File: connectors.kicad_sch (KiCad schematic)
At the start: 2 parts, among them J1 0436500200, J2 0430450200

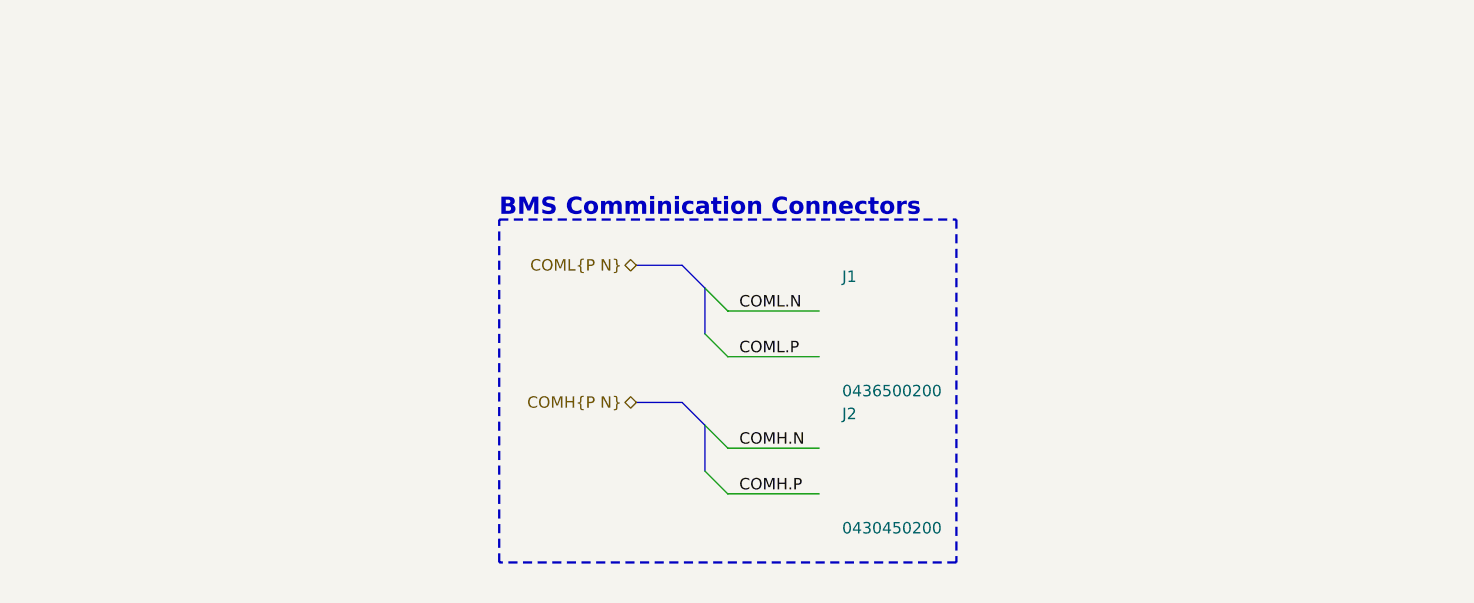
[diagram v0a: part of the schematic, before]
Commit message: SCH[Connector]: Added tim board to board connector.
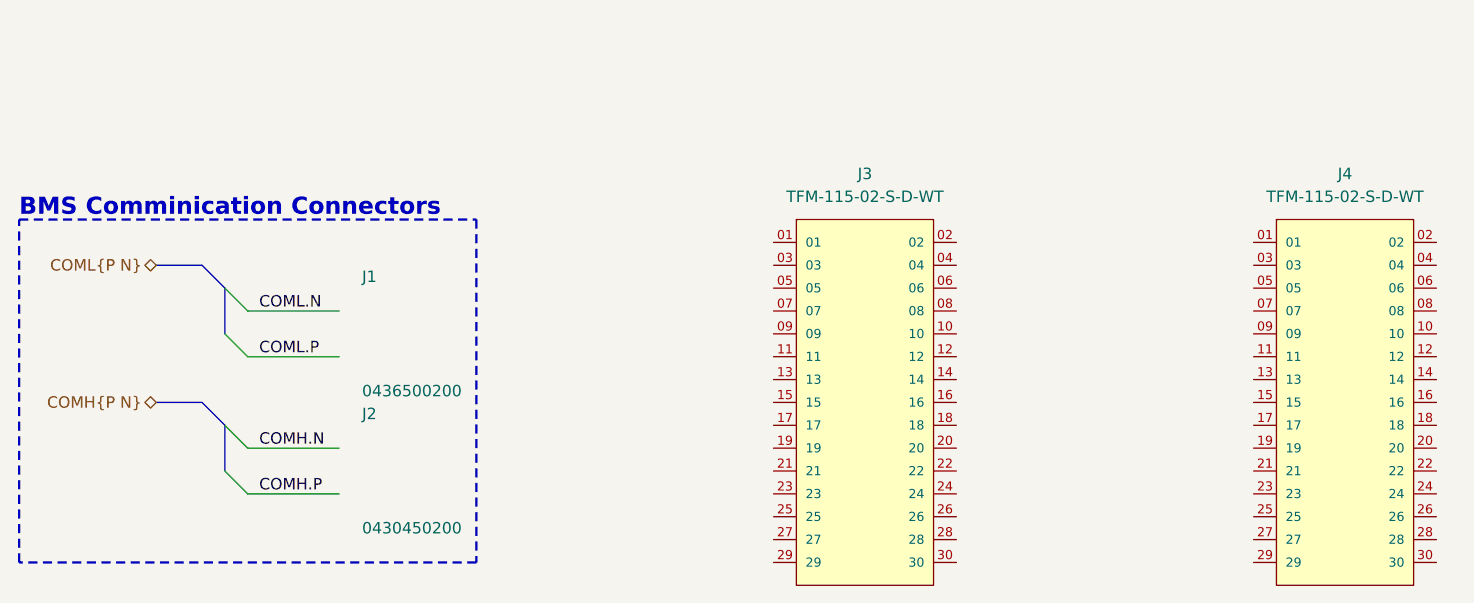
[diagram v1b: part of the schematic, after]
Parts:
- added J3, J4: TFM-115-02-S-D-WT, remote_tfm-115-02-s-d-wt:SAMTEC_TFM-115-02-S-D-WT, symbol remote_tfm-115-02-s-d-wt:TFM-115-02-S-D-WT

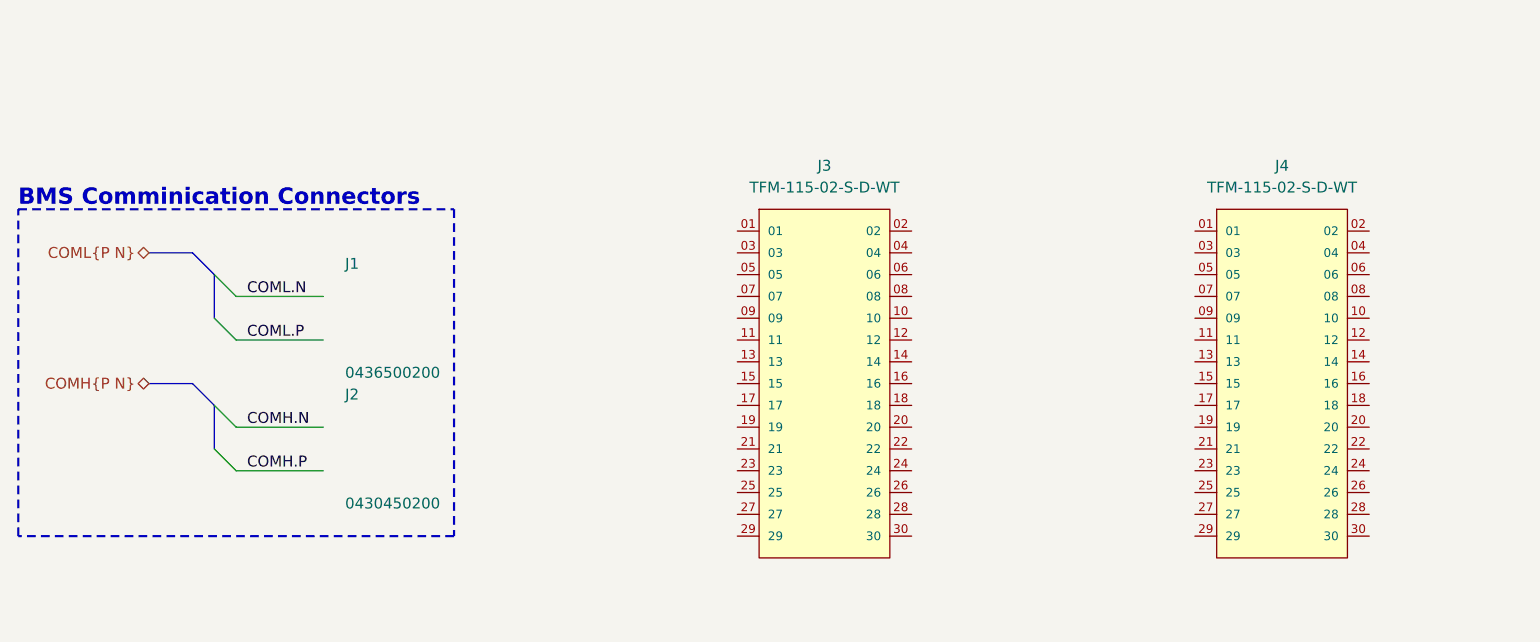
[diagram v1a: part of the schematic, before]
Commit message: SCH[Connecotr]: Added tim pinout.
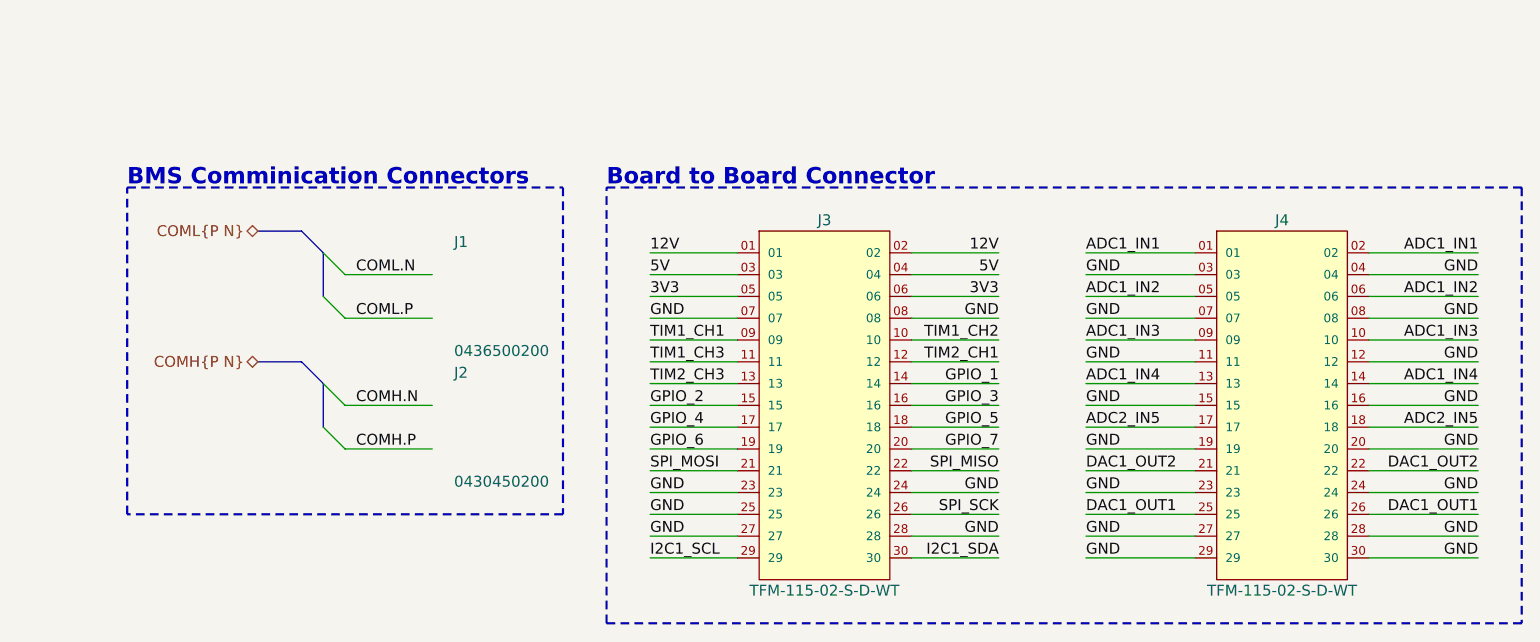
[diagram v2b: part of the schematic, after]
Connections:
- net ADC1_IN1: now reaches J4.01
- net ADC1_IN1: now also J4.02
- net GND: now reaches J4.03
- net GND: now also J3.07, J3.08, J3.23, J3.24, J3.25, J3.27, J3.28, J4.04, J4.07, J4.08, J4.11, J4.12, J4.15, J4.16, J4.19, J4.20, J4.23, J4.24, J4.27, J4.28, J4.29, J4.30
- net ADC1_IN2: now reaches J4.05
- net ADC1_IN2: now also J4.06
- net ADC1_IN3: now reaches J4.09
- net ADC1_IN3: now also J4.10
- net ADC1_IN4: now reaches J4.13
- net ADC1_IN4: now also J4.14
- net ADC2_IN5: now reaches J4.17
- net ADC2_IN5: now also J4.18
- net DAC1_OUT2: now reaches J4.21
- net DAC1_OUT2: now also J4.22
- net DAC1_OUT1: now reaches J4.25
- net DAC1_OUT1: now also J4.26
- net 12V: now reaches J3.01
- net 12V: now also J3.02
- net 5V: now reaches J3.03
- net 5V: now also J3.04
- net 3V3: now reaches J3.05
- net 3V3: now also J3.06
- net TIM1_CH1: now reaches J3.09
- net TIM1_CH2: now reaches J3.10
- net TIM1_CH3: now reaches J3.11
- net TIM2_CH1: now reaches J3.12
- net TIM2_CH3: now reaches J3.13
- net GPIO_1: now reaches J3.14
- net GPIO_2: now reaches J3.15
- net GPIO_3: now reaches J3.16
- net GPIO_4: now reaches J3.17
- net GPIO_5: now reaches J3.18
- net GPIO_6: now reaches J3.19
- net GPIO_7: now reaches J3.20
- net SPI_MOSI: now reaches J3.21
- net SPI_MISO: now reaches J3.22
- net SPI_SCK: now reaches J3.26
- net I2C1_SCL: now reaches J3.29
- net I2C1_SDA: now reaches J3.30
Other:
- note added: "Board to Board Connector"
- moved on the sheet: J3, J4

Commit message: SCH[Power]: Adding caps, resistors based off datasheet recs.
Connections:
- net 12V renamed +12V
- net 3V3 renamed +3V3
- net 5V renamed +5V
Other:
- note added: "Power"
- moved on the sheet: J3, J4

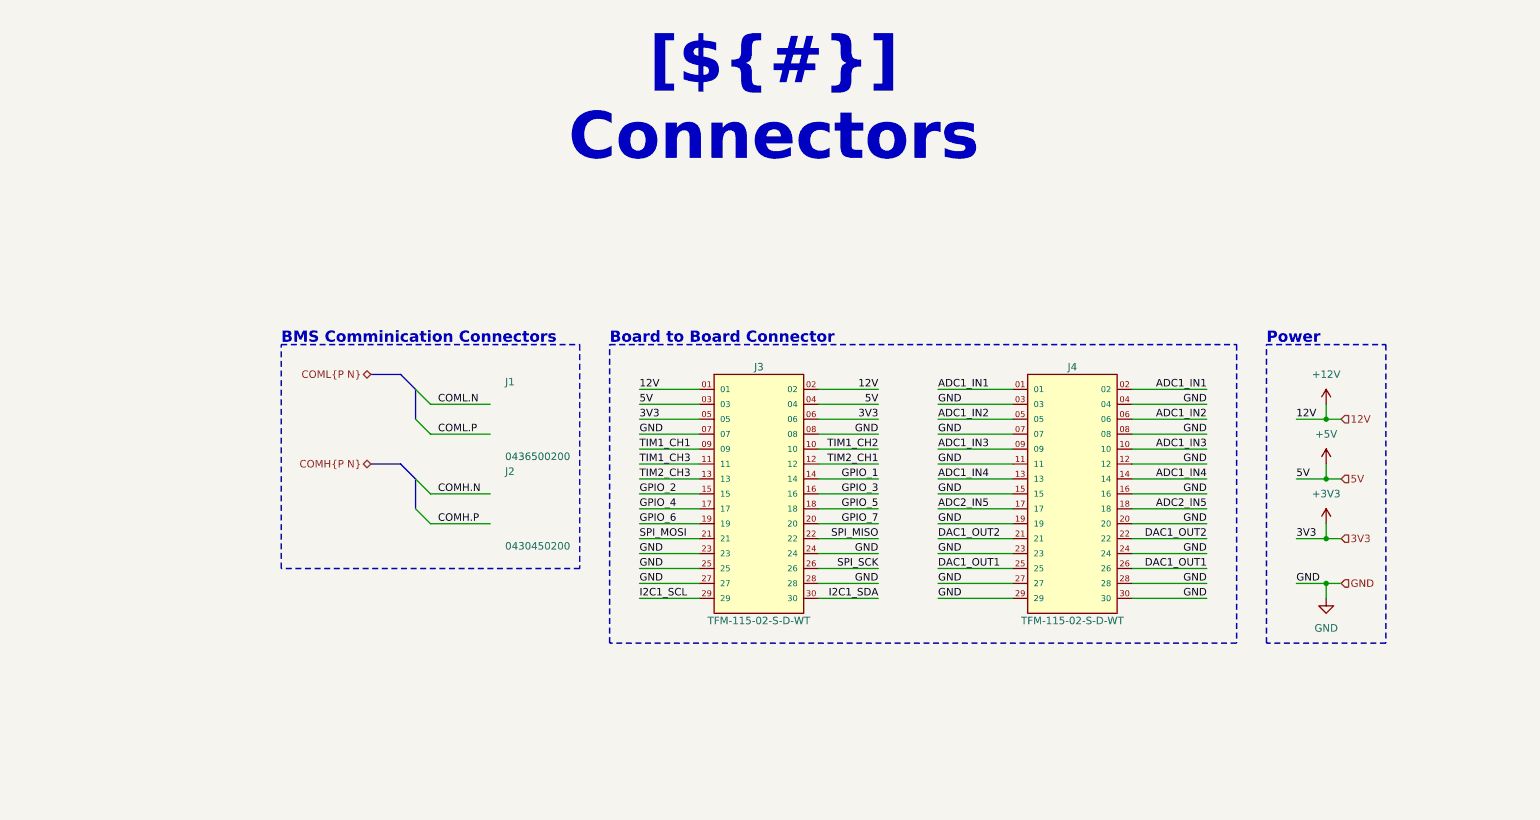
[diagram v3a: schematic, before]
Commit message: SCH[Pages, Chips]: Created page setup, and placed main IC's.
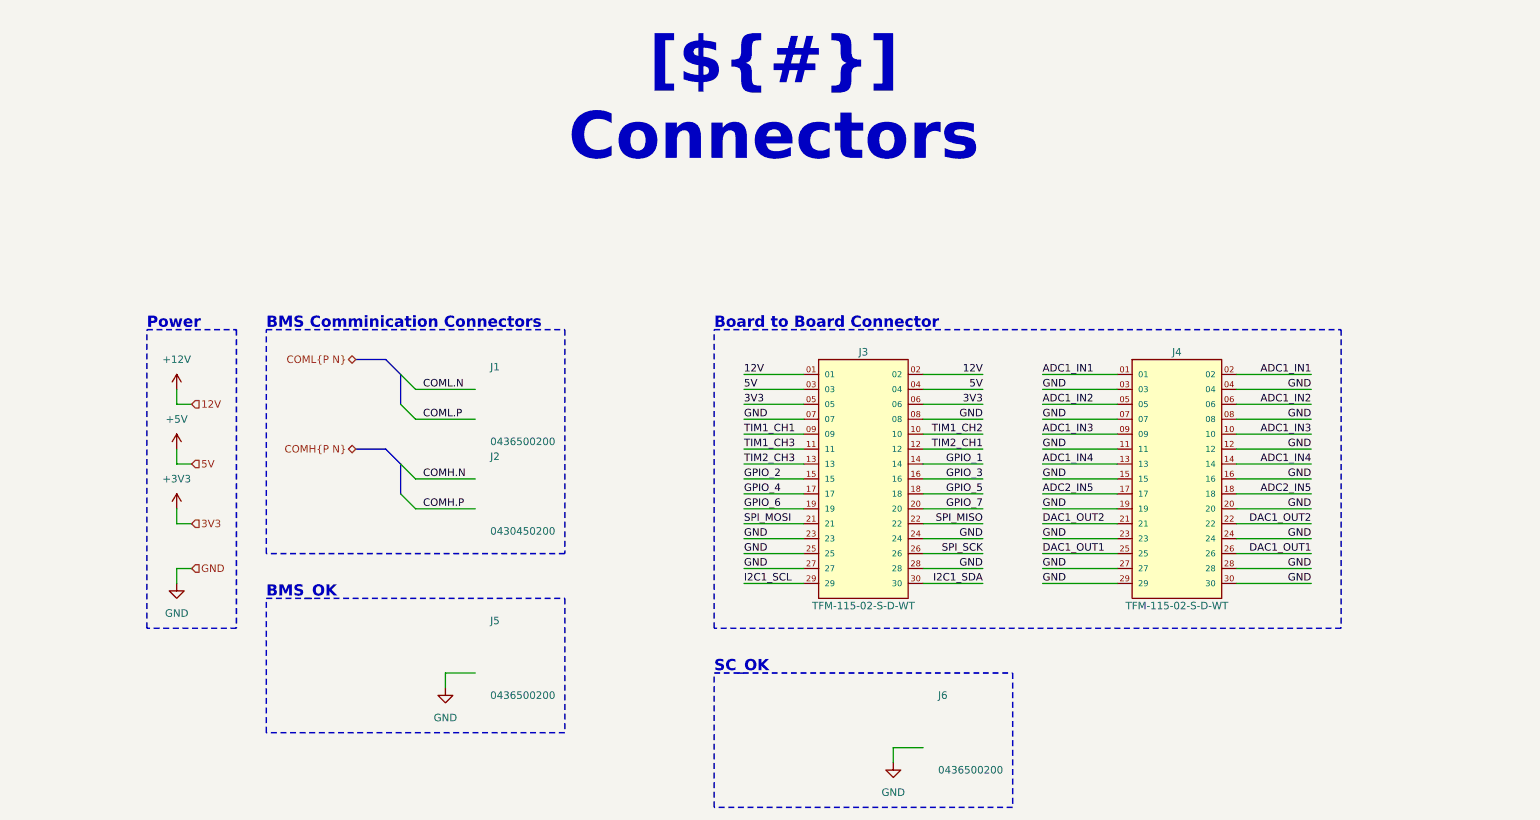
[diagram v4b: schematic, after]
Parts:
- added J5, J6: 0436500200, remote_0436500200:CONN_SD-43650-001_02_MOL, symbol remote_0436500200:0436500200
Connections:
- net GND: now also J5.2, J6.2
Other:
- note added: "BMS_OK"
- note added: "SC_OK"
- moved on the sheet: J3, J4

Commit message: SCH[Labels]: Working on pinout for tim.
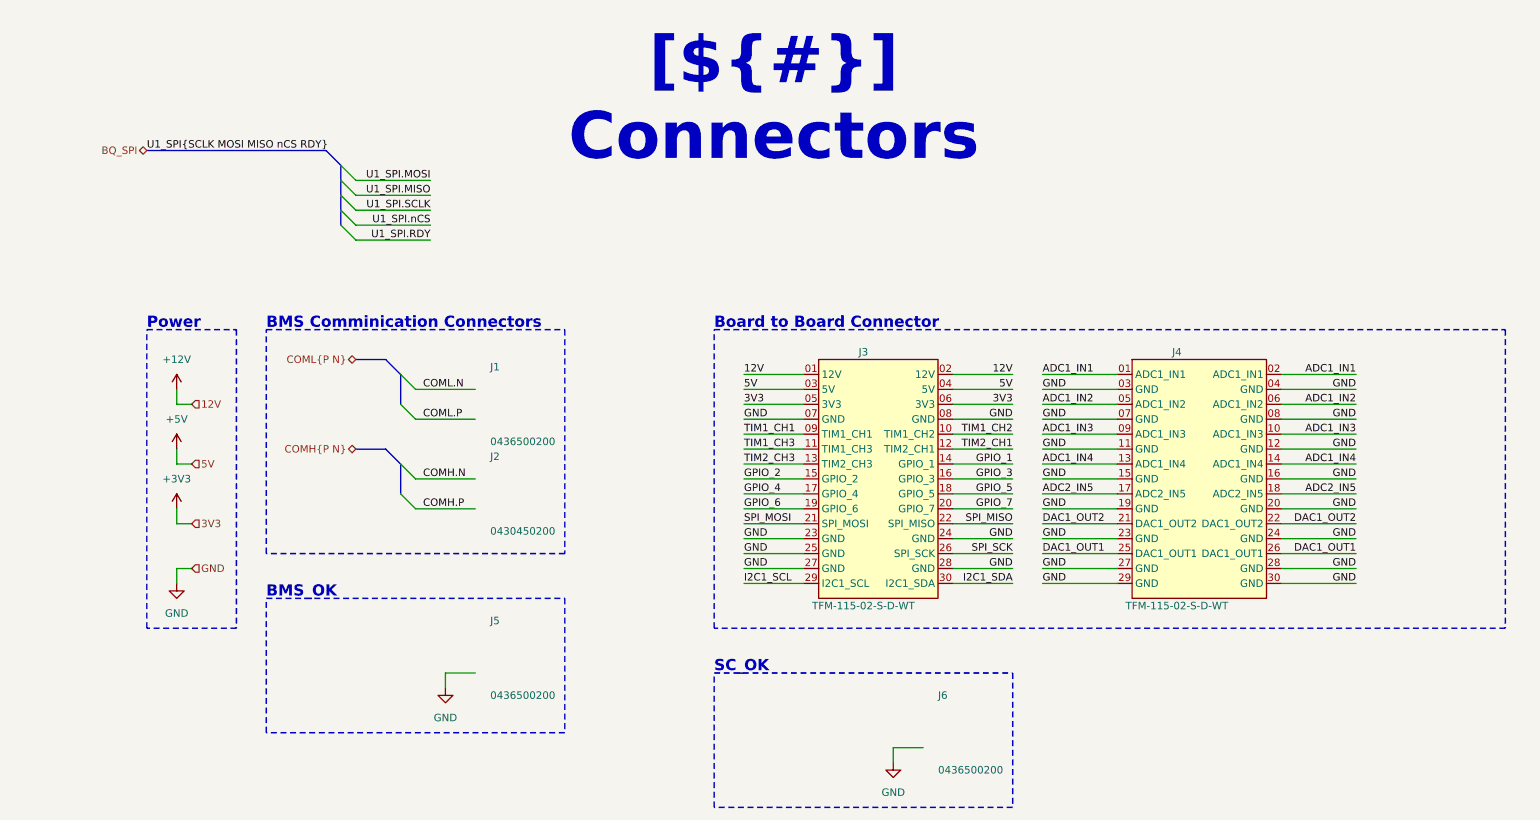
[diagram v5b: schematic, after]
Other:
- moved on the sheet: J3, J4

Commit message: SCH[Sens & Inputs, Logic]: Started on sens and inputs condtiong, Logic page drawn. Need to add notes still.
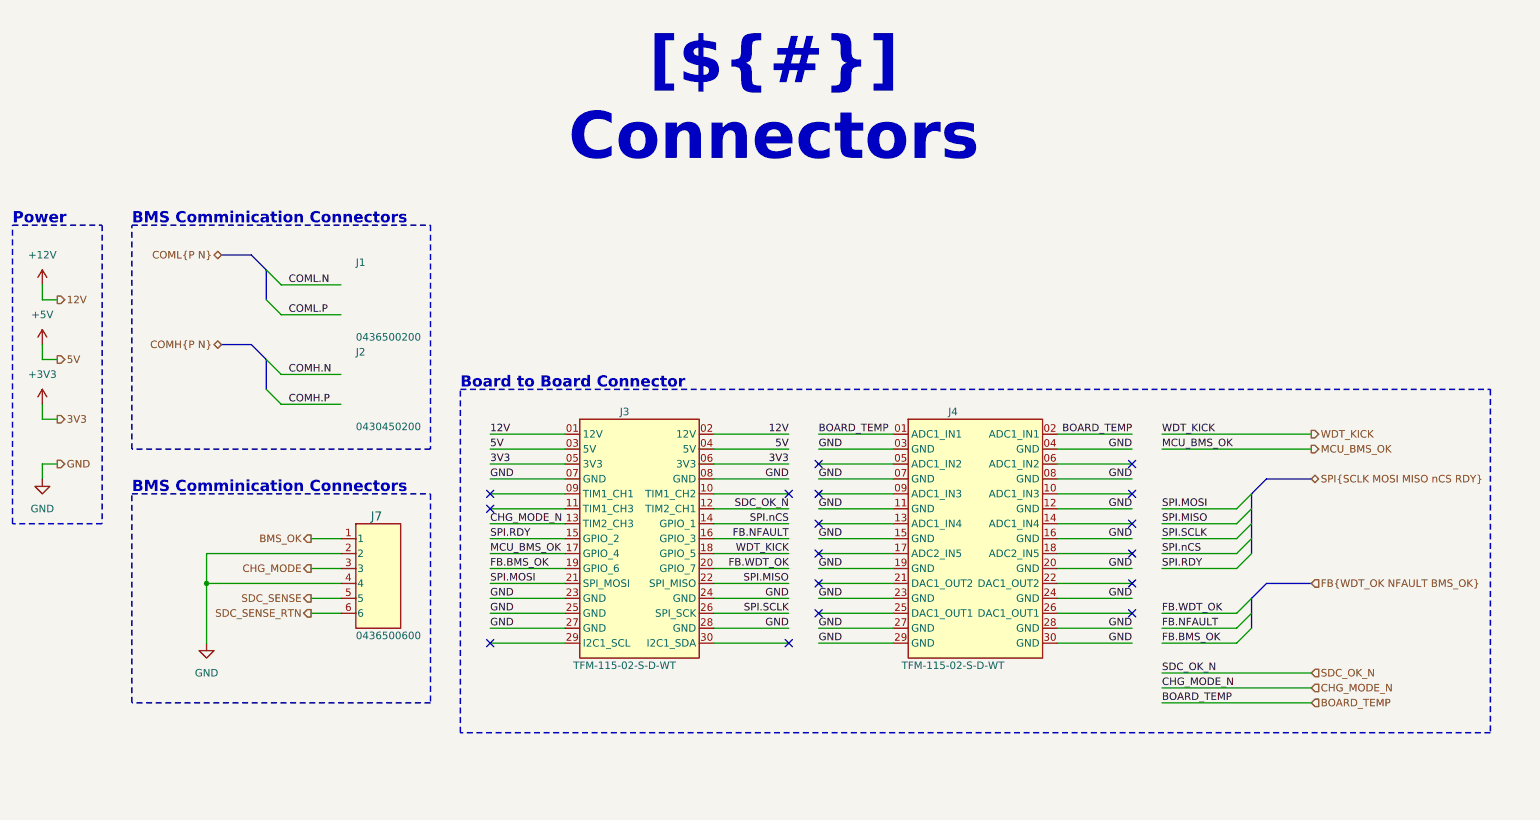
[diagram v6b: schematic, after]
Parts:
- removed J5, J6: 0436500200, remote_0436500200:CONN_SD-43650-001_02_MOL, symbol remote_0436500200:0436500200
- added J7: 0436500600, remote_0436500600:CONN_SD-43650-001_06_MOL, symbol remote_0436500600:0436500600
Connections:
- net GND: now also J7.2, J7.4
- net ADC1_IN1 renamed BOARD_TEMP
- net ADC1_IN2: no longer names the net of J4.05 (ADC1_IN2)
- net ADC1_IN2: no longer J4.06 (ADC1_IN2)
- net ADC1_IN3: no longer names the net of J4.09 (ADC1_IN3)
- net ADC1_IN3: no longer J4.10 (ADC1_IN3)
- net ADC1_IN4: no longer names the net of J4.13 (ADC1_IN4)
- net ADC1_IN4: no longer J4.14 (ADC1_IN4)
- net ADC2_IN5: no longer names the net of J4.17 (ADC2_IN5)
- net ADC2_IN5: no longer J4.18 (ADC2_IN5)
- net DAC1_OUT1: no longer names the net of J4.25 (DAC1_OUT1)
- net DAC1_OUT1: no longer J4.26 (DAC1_OUT1)
- net DAC1_OUT2: no longer names the net of J4.21 (DAC1_OUT2)
- net DAC1_OUT2: no longer J4.22 (DAC1_OUT2)
- net GPIO_1 renamed SPI.nCS
- net GPIO_2 renamed SPI.RDY
- net GPIO_3 renamed FB.NFAULT
- net GPIO_4 renamed MCU_BMS_OK
- net GPIO_5 renamed WDT_KICK
- net GPIO_6 renamed FB.BMS_OK
- net GPIO_7 renamed FB.WDT_OK
- net I2C1_SCL: no longer names the net of J3.29 (I2C1_SCL)
- net I2C1_SDA: no longer names the net of J3.30 (I2C1_SDA)
- net SPI_MISO renamed SPI.MISO
- net SPI_MOSI renamed SPI.MOSI
- net SPI_SCK renamed SPI.SCLK
- net TIM1_CH1: no longer names the net of J3.09 (TIM1_CH1)
- net TIM1_CH2: no longer names the net of J3.10 (TIM1_CH2)
- net TIM1_CH3: no longer names the net of J3.11 (TIM1_CH3)
- net TIM2_CH1 renamed SDC_OK_N
- net TIM2_CH3 renamed CHG_MODE_N
- new net BMS_OK: J7.1
- new net CHG_MODE: J7.3
- new net SDC_SENSE: J7.5
- new net SDC_SENSE_RTN: J7.6
- no-connect marks 0 -> 17
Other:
- note removed: "BMS_OK"
- note removed: "SC_OK"
- moved on the sheet: J3, J4

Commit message: SCH[Logic, Connectors]: Removed watchdog timer going to use just stm32 interal watchdog, and com master faults. This is to simplfiy hardware less parts not needed. Adding DNP conector for halleffect sensor.
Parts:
- added J5: 0436500400, remote_0436500400:CONN_SD-43650-001_04_MOL, symbol remote_0436500400:0436500400
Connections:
- net FB.WDT_OK is gone; now on net SDC_OK_N: J3.20 (GPIO_7)
- net WDT_KICK is gone; now on net CHG_MODE_N: J3.18 (GPIO_5)
- net CHG_MODE_N: no longer J3.13 (TIM2_CH3)
- net SDC_OK_N: no longer J3.12 (TIM2_CH1)
- no-connect marks 17 -> 19
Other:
- moved on the sheet: J3, J4
